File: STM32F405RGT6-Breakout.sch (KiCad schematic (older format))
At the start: 29 parts

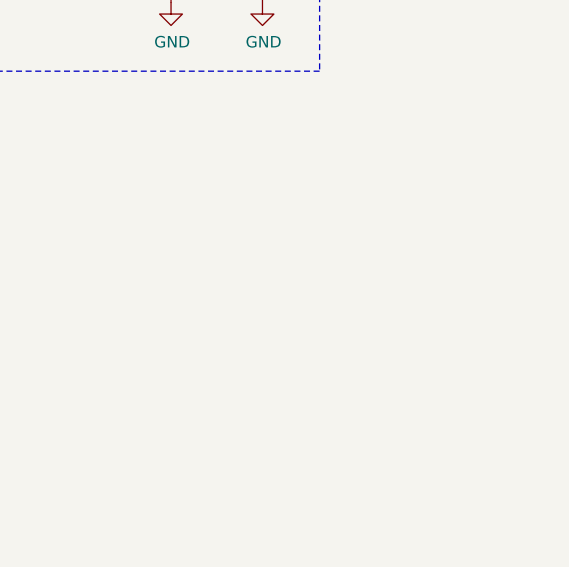
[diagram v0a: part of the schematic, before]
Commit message: - add JTAG/SWD connector - configure USB pins on chip
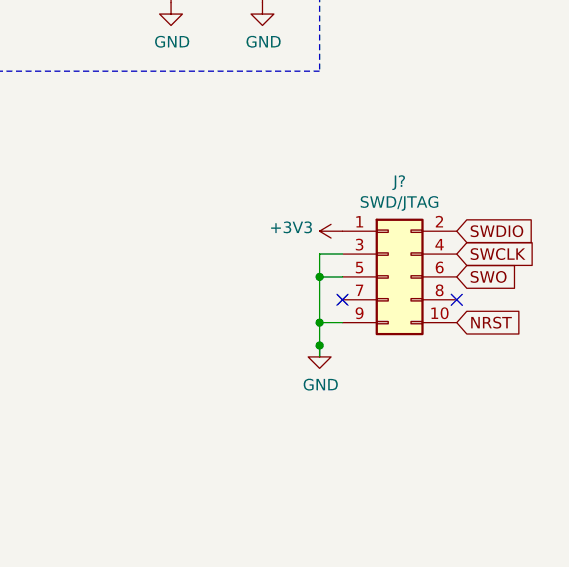
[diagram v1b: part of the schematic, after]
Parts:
- added J?: SWD/JTAG, symbol Connector_Generic:Conn_02x05_Odd_Even
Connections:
- net +3V3: now also J?.1 (Pin_1)
- net GND: now also J?.3 (Pin_3), J?.5 (Pin_5), J?.9 (Pin_9)
- net NRST: now also J?.10 (Pin_10)
- net SWCLK: now also J?.4 (Pin_4)
- net SWDIO: now also J?.2 (Pin_2)
- net SWO: now also J?.6 (Pin_6)
- no-connect marks 0 -> 2
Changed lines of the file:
@@
 	3100 1350 3350 1350
 $Comp
-L power:GND #PWR?
+L power:GND #PWR0101
 U 1 1 6194D181
 P 1600 2050
-F 0 "#PWR?" H 1600 1800 50  0001 C CNN
+F 0 "#PWR0101" H 1600 1800 50  0001 C CNN
 F 1 "GND" H 1605 1877 50  0000 C CNN
 F 2 "" H 1600 2050 50  0001 C CNN
@@
 $EndComp
 $Comp
-L power:VCC #PWR?
+L power:VCC #PWR0102
 U 1 1 6195256A
 P 950 1350
-F 0 "#PWR?" H 950 1200 50  0001 C CNN
+F 0 "#PWR0102" H 950 1200 50  0001 C CNN
 F 1 "VCC" H 965 1523 50  0000 C CNN
 F 2 "" H 950 1350 50  0001 C CNN
@@
 Off when gate is high,\ni.e. supply polarity \nis reversed
 $Comp
-L power:GND #PWR?
+L power:GND #PWR0103
 U 1 1 6194DC8B
 P 3800 1800
-F 0 "#PWR?" H 3800 1550 50  0001 C CNN
+F 0 "#PWR0103" H 3800 1550 50  0001 C CNN
 F 1 "GND" H 3805 1627 50  0000 C CNN
 F 2 "" H 3800 1800 50  0001 C CNN
@@
 	4350 1350 4200 1350
 $Comp
-L power:+3V3 #PWR?
+L power:+3V3 #PWR0104
 U 1 1 61961ED5
 P 4350 1350
-F 0 "#PWR?" H 4350 1200 50  0001 C CNN
+F 0 "#PWR0104" H 4350 1200 50  0001 C CNN
 F 1 "+3V3" H 4365 1523 50  0000 C CNN
 F 2 "" H 4350 1350 50  0001 C CNN
@@
 	650  750  4650 750
 $Comp
-L power:+3V3 #PWR?
+L power:+3V3 #PWR0105
 U 1 1 61974FD8
 P 6050 2400
-F 0 "#PWR?" H 6050 2250 50  0001 C CNN
+F 0 "#PWR0105" H 6050 2250 50  0001 C CNN
 F 1 "+3V3" H 6065 2573 50  0000 C CNN
 F 2 "" H 6050 2400 50  0001 C CNN
@@
 Connection ~ 6050 2450
 $Comp
-L power:+3V3 #PWR?
+L power:+3V3 #PWR0106
 U 1 1 6197E4D1
 P 8500 1050
-F 0 "#PWR?" H 8500 900 50  0001 C CNN
+F 0 "#PWR0106" H 8500 900 50  0001 C CNN
 F 1 "+3V3" H 8515 1223 50  0000 C CNN
 F 2 "" H 8500 1050 50  0001 C CNN
@@
 	8500 1200 8850 1200
 $Comp
-L power:+3.3VA #PWR?
+L power:+3.3VA #PWR0107
 U 1 1 61983E43
 P 6550 2400
-F 0 "#PWR?" H 6550 2250 50  0001 C CNN
+F 0 "#PWR0107" H 6550 2250 50  0001 C CNN
 F 1 "+3.3VA" H 6565 2573 50  0000 C CNN
 F 2 "" H 6550 2400 50  0001 C CNN
@@
 	6550 2400 6550 2500
 $Comp
-L power:+3.3VA #PWR?
+L power:+3.3VA #PWR0108
 U 1 1 61985D6F
 P 9600 1050
-F 0 "#PWR?" H 9600 900 50  0001 C CNN
+F 0 "#PWR0108" H 9600 900 50  0001 C CNN
 F 1 "+3.3VA" H 9615 1223 50  0000 C CNN
 F 2 "" H 9600 1050 50  0001 C CNN
@@
 Connection ~ 9600 1200
 $Comp
-L power:GND #PWR?
+L power:GND #PWR0109
 U 1 1 6198711A
 P 9200 1500
-F 0 "#PWR?" H 9200 1250 50  0001 C CNN
+F 0 "#PWR0109" H 9200 1250 50  0001 C CNN
 F 1 "GND" H 9205 1327 50  0000 C CNN
 F 2 "" H 9200 1500 50  0001 C CNN
@@
 $EndComp
 $Comp
-L power:GND #PWR?
+L power:GND #PWR0110
 U 1 1 61987910
 P 9600 1500
-F 0 "#PWR?" H 9600 1250 50  0001 C CNN
+F 0 "#PWR0110" H 9600 1250 50  0001 C CNN
 F 1 "GND" H 9605 1327 50  0000 C CNN
 F 2 "" H 9600 1500 50  0001 C CNN
@@
 	5300 2000 5650 2000
 $Comp
-L power:+3V3 #PWR?
+L power:+3V3 #PWR0111
 U 1 1 619B12B5
 P 7750 1700
-F 0 "#PWR?" H 7750 1550 50  0001 C CNN
+F 0 "#PWR0111" H 7750 1550 50  0001 C CNN
 F 1 "+3V3" H 7765 1873 50  0000 C CNN
 F 2 "" H 7750 1700 50  0001 C CNN
@@
 	4950 1700 4950 1750
 $Comp
-L power:GND #PWR?
+L power:GND #PWR0112
 U 1 1 619B2039
 P 7750 2000
-F 0 "#PWR?" H 7750 1750 50  0001 C CNN
+F 0 "#PWR0112" H 7750 1750 50  0001 C CNN
 F 1 "GND" H 7755 1827 50  0000 C CNN
 F 2 "" H 7750 2000 50  0001 C CNN
@@
 	5300 3200 5550 3200
 $Comp
-L power:GND #PWR?
+L power:GND #PWR0113
 U 1 1 619D0066
 P 4950 3500
-F 0 "#PWR?" H 4950 3250 50  0001 C CNN
+F 0 "#PWR0113" H 4950 3250 50  0001 C CNN
 F 1 "GND" H 4955 3327 50  0000 C CNN
 F 2 "" H 4950 3500 50  0001 C CNN
@@
 $EndComp
 $Comp
-L power:GND #PWR?
+L power:GND #PWR0114
 U 1 1 619D8425
 P 3800 4650
-F 0 "#PWR?" H 3800 4400 50  0001 C CNN
+F 0 "#PWR0114" H 3800 4400 50  0001 C CNN
 F 1 "GND" H 3805 4477 50  0000 C CNN
 F 2 "" H 3800 4650 50  0001 C CNN
@@
 BOOT0
 $Comp
-L power:GND #PWR?
+L power:GND #PWR0115
 U 1 1 61A1C688
 P 7650 3650
-F 0 "#PWR?" H 7650 3400 50  0001 C CNN
+F 0 "#PWR0115" H 7650 3400 50  0001 C CNN
 F 1 "GND" H 7655 3477 50  0000 C CNN
 F 2 "" H 7650 3650 50  0001 C CNN
@@
 $EndComp
 $Comp
-L power:GND #PWR?
+L power:GND #PWR0116
 U 1 1 61A1CBA1
 P 7950 3650
-F 0 "#PWR?" H 7950 3400 50  0001 C CNN
+F 0 "#PWR0116" H 7950 3400 50  0001 C CNN
 F 1 "GND" H 7955 3477 50  0000 C CNN
 F 2 "" H 7950 3650 50  0001 C CNN
@@
 SWO
 $Comp
-L power:GND #PWR?
+L power:GND #PWR0117
 U 1 1 619D0B27
 P 5300 3500
-F 0 "#PWR?" H 5300 3250 50  0001 C CNN
+F 0 "#PWR0117" H 5300 3250 50  0001 C CNN
 F 1 "GND" H 5305 3327 50  0000 C CNN
 F 2 "" H 5300 3500 50  0001 C CNN
@@
 $EndComp
 $Comp
-L power:GND #PWR?
+L power:GND #PWR0118
 U 1 1 61A2A7A4
 P 6150 6200
-F 0 "#PWR?" H 6150 5950 50  0001 C CNN
+F 0 "#PWR0118" H 6150 5950 50  0001 C CNN
 F 1 "GND" H 6155 6027 50  0000 C CNN
 F 2 "" H 6150 6200 50  0001 C CNN
@@
 Text Notes 5000 1650 0    50   ~ 0
 Decoupling: 2x100u per VDD + 10u bulk close to chip
+$Comp
+L Connector_Generic:Conn_02x05_Odd_Even J?
+U 1 1 61A3C8B7
+P 10150 2700
+F 0 "J?" H 10200 3117 50  0000 C CNN
+F 1 "SWD/JTAG" H 10200 3026 50  0000 C CNN
+F 2 "" H 10150 2700 50  0001 C CNN
+F 3 "~" H 10150 2700 50  0001 C CNN
+	1    10150 2700
+	1    0    0    -1
+$EndComp
+$Comp
+L power:+3V3 #PWR?
+U 1 1 61A41135
+P 9950 2500
+F 0 "#PWR?" H 9950 2350 50  0001 C CNN
+F 1 "+3V3" V 9965 2628 50  0000 L CNN
+F 2 "" H 9950 2500 50  0001 C CNN
+F 3 "" H 9950 2500 50  0001 C CNN
+	1    9950 2500
+	0    -1   -1   0
+$EndComp
+$Comp
+L power:GND #PWR?
+U 1 1 61A43965
+P 9850 3000
+F 0 "#PWR?" H 9850 2750 50  0001 C CNN
+F 1 "GND" H 9855 2827 50  0000 C CNN
+F 2 "" H 9850 3000 50  0001 C CNN
+F 3 "" H 9850 3000 50  0001 C CNN
+	1    9850 3000
+	1    0    0    -1
+$EndComp
+NoConn ~ 10450 2800
+NoConn ~ 9950 2800
+Text GLabel 10450 2700 2    50   Input ~ 0
+SWO
+Text GLabel 10450 2500 2    50   Input ~ 0
+SWDIO
+Text GLabel 10450 2600 2    50   Input ~ 0
+SWCLK
+Wire Wire Line
+	9850 2600 9850 2700
+Wire Wire Line
+	9850 2600 9950 2600
+Wire Wire Line
+	9950 2900 9850 2900
+Connection ~ 9850 2900
+Wire Wire Line
+	9850 2900 9850 3000
+Wire Wire Line
+	9950 2700 9850 2700
+Connection ~ 9850 2700
+Wire Wire Line
+	9850 2700 9850 2900
+Connection ~ 9850 3000
+Wire Wire Line
+	9850 3000 9850 3050
+Text GLabel 10450 2900 2    50   Input ~ 0
+NRST
 $EndSCHEMATC

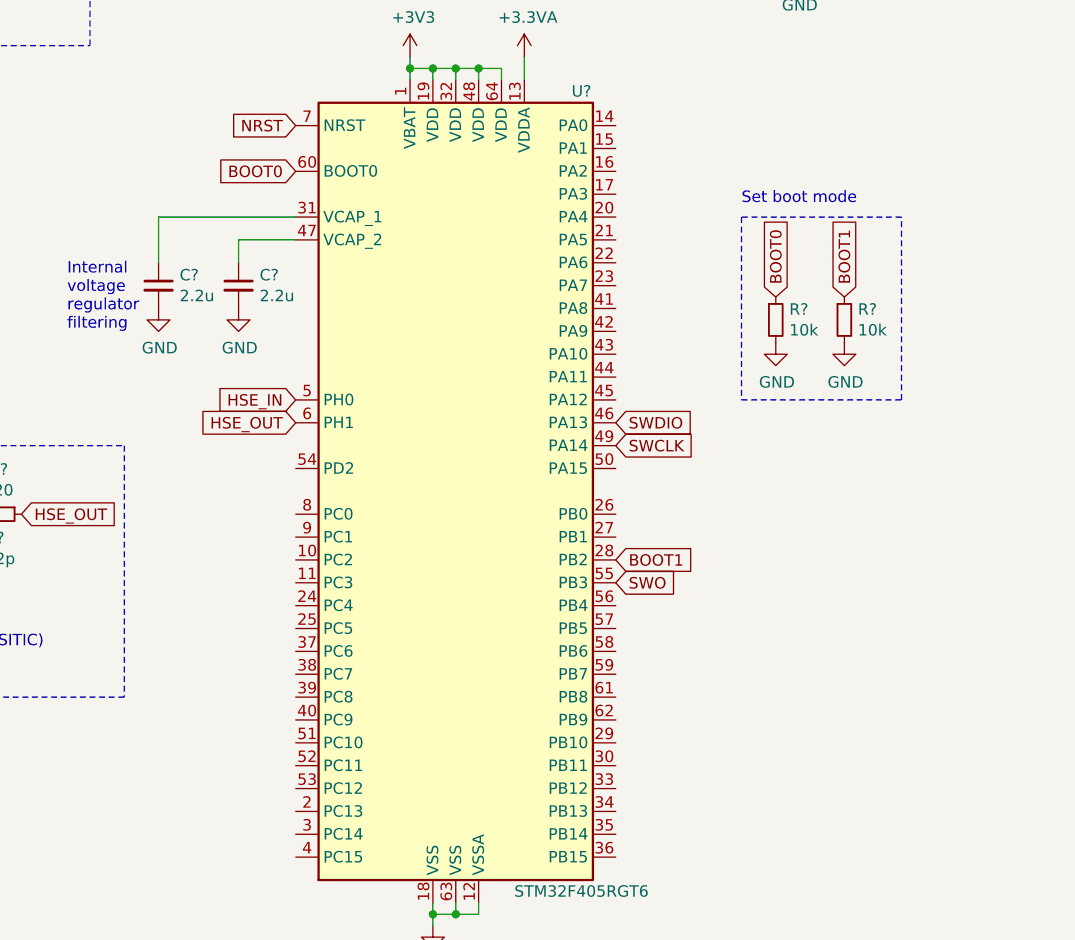
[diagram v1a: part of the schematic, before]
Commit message: communication pins labeled
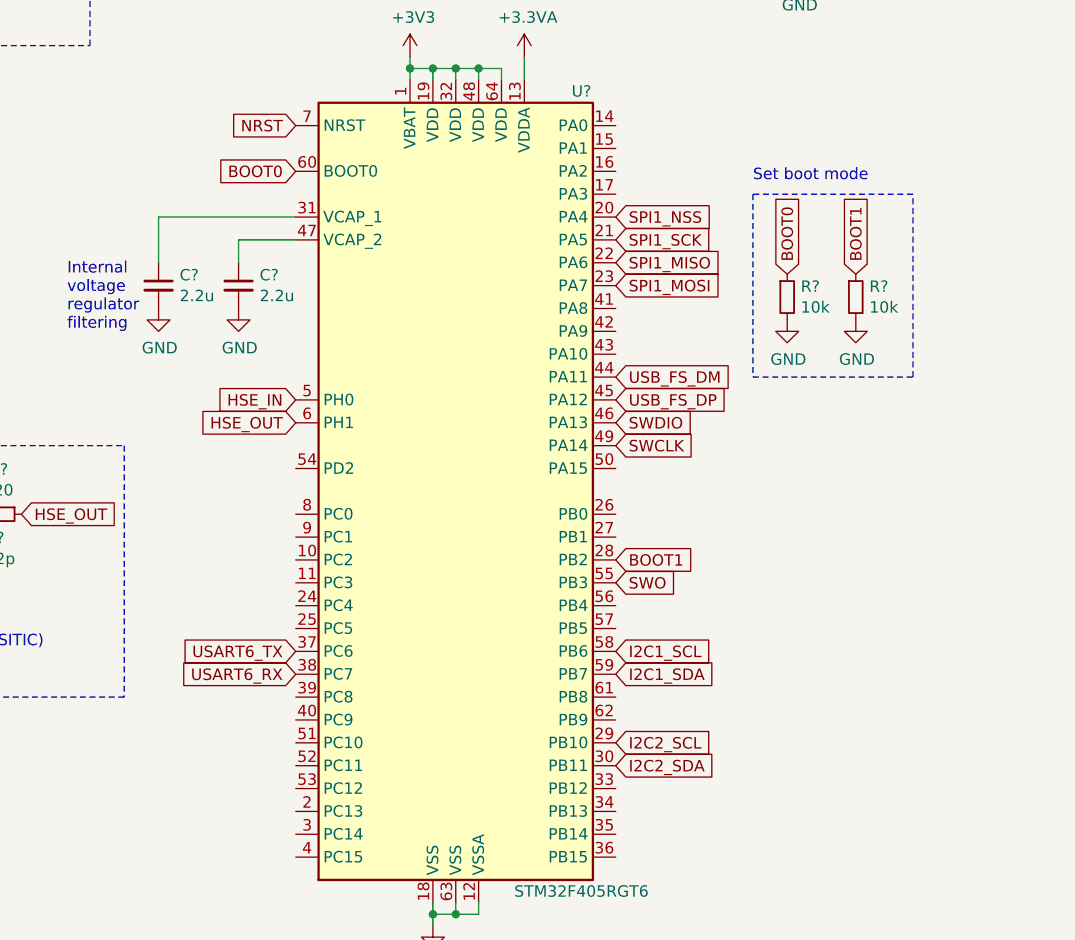
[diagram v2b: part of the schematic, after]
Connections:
- net SPI1_NSS: now reaches U?.20 (PA4)
- net SPI1_SCK: now reaches U?.21 (PA5)
- net SPI1_MISO: now reaches U?.22 (PA6)
- net SPI1_MOSI: now reaches U?.23 (PA7)
- net I2C2_SCL: now reaches U?.29 (PB10)
- net I2C2_SDA: now reaches U?.30 (PB11)
- net USART6_TX: now reaches U?.37 (PC6)
- net USART6_RX: now reaches U?.38 (PC7)
- net USB_FS_DM: now reaches U?.44 (PA11)
- net USB_FS_DP: now reaches U?.45 (PA12)
- net I2C1_SCL: now reaches U?.58 (PB6)
- net I2C1_SDA: now reaches U?.59 (PB7)
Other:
- moved on the sheet: R?
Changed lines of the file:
@@
 L Device:R_Small R?
 U 1 1 61A1AA95
-P 7650 3550
-F 0 "R?" H 7709 3596 50  0000 L CNN
-F 1 "10k" H 7709 3505 50  0000 L CNN
-F 2 "" H 7650 3550 50  0001 C CNN
-F 3 "~" H 7650 3550 50  0001 C CNN
-	1    7650 3550
+P 7700 3450
+F 0 "R?" H 7759 3496 50  0000 L CNN
+F 1 "10k" H 7759 3405 50  0000 L CNN
+F 2 "" H 7700 3450 50  0001 C CNN
+F 3 "~" H 7700 3450 50  0001 C CNN
+	1    7700 3450
 	1    0    0    -1
 $EndComp
@@
 L Device:R_Small R?
 U 1 1 61A1B70C
-P 7950 3550
-F 0 "R?" H 8009 3596 50  0000 L CNN
-F 1 "10k" H 8009 3505 50  0000 L CNN
-F 2 "" H 7950 3550 50  0001 C CNN
-F 3 "~" H 7950 3550 50  0001 C CNN
-	1    7950 3550
+P 8000 3450
+F 0 "R?" H 8059 3496 50  0000 L CNN
+F 1 "10k" H 8059 3405 50  0000 L CNN
+F 2 "" H 8000 3450 50  0001 C CNN
+F 3 "~" H 8000 3450 50  0001 C CNN
+	1    8000 3450
 	1    0    0    -1
 $EndComp
-Text GLabel 7950 3450 1    50   Input ~ 0
+Text GLabel 8000 3350 1    50   Input ~ 0
 BOOT1
-Text GLabel 7650 3450 1    50   Input ~ 0
+Text GLabel 7700 3350 1    50   Input ~ 0
 BOOT0
 $Comp
 L power:GND #PWR0115
 U 1 1 61A1C688
-P 7650 3650
-F 0 "#PWR0115" H 7650 3400 50  0001 C CNN
-F 1 "GND" H 7655 3477 50  0000 C CNN
-F 2 "" H 7650 3650 50  0001 C CNN
-F 3 "" H 7650 3650 50  0001 C CNN
-	1    7650 3650
+P 7700 3550
+F 0 "#PWR0115" H 7700 3300 50  0001 C CNN
+F 1 "GND" H 7705 3377 50  0000 C CNN
+F 2 "" H 7700 3550 50  0001 C CNN
+F 3 "" H 7700 3550 50  0001 C CNN
+	1    7700 3550
 	1    0    0    -1
 $EndComp
@@
 L power:GND #PWR0116
 U 1 1 61A1CBA1
-P 7950 3650
-F 0 "#PWR0116" H 7950 3400 50  0001 C CNN
-F 1 "GND" H 7955 3477 50  0000 C CNN
-F 2 "" H 7950 3650 50  0001 C CNN
-F 3 "" H 7950 3650 50  0001 C CNN
-	1    7950 3650
+P 8000 3550
+F 0 "#PWR0116" H 8000 3300 50  0001 C CNN
+F 1 "GND" H 8005 3377 50  0000 C CNN
+F 2 "" H 8000 3550 50  0001 C CNN
+F 3 "" H 8000 3550 50  0001 C CNN
+	1    8000 3550
 	1    0    0    -1
 $EndComp
 Wire Notes Line
-	7500 3100 7500 3900
+	7550 3000 7550 3800
 Wire Notes Line
-	7500 3900 8200 3900
+	7550 3800 8250 3800
 Wire Notes Line
-	8200 3900 8200 3100
+	8250 3800 8250 3000
 Wire Notes Line
-	8200 3100 7500 3100
-Text Notes 7500 3050 0    50   ~ 0
+	8250 3000 7550 3000
+Text Notes 7550 2950 0    50   ~ 0
 Set boot mode
 Text Notes 8400 750  0    50   ~ 0
@@
 Text GLabel 10450 2900 2    50   Input ~ 0
 NRST
+Text GLabel 6950 3900 2    50   Input ~ 0
+USB_FS_DP
+Text GLabel 6950 3800 2    50   Input ~ 0
+USB_FS_DM
+Text GLabel 5550 5100 0    50   Input ~ 0
+USART6_RX
+Text GLabel 5550 5000 0    50   Input ~ 0
+USART6_TX
+Text GLabel 6950 5500 2    50   Input ~ 0
+I2C2_SDA
+Text GLabel 6950 5400 2    50   Input ~ 0
+I2C2_SCL
+Text GLabel 6950 5100 2    50   Input ~ 0
+I2C1_SDA
+Text GLabel 6950 5000 2    50   Input ~ 0
+I2C1_SCL
+Text GLabel 6950 3100 2    50   Input ~ 0
+SPI1_NSS
+Text GLabel 6950 3200 2    50   Input ~ 0
+SPI1_SCK
+Text GLabel 6950 3400 2    50   Input ~ 0
+SPI1_MOSI
+Text GLabel 6950 3300 2    50   Input ~ 0
+SPI1_MISO
 $EndSCHEMATC
